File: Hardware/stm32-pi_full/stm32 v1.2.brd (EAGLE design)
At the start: 131.4 x 105.8 mm, 287 parts, among them J1 JUMPER-SMT_2_NC_TRACE_NO-SILK, Q1 PNP, Q2 NPN, Q3 NPN, U1 ESP32-WROOM-32D

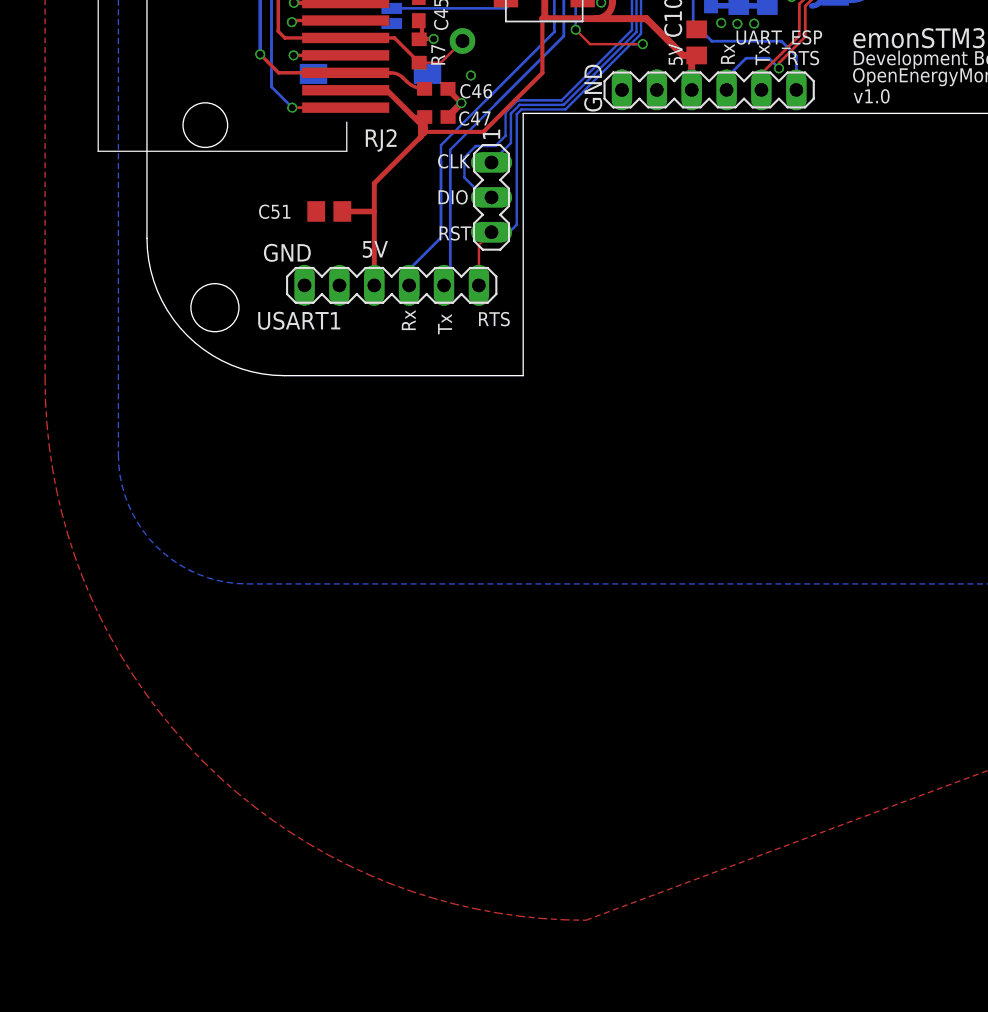
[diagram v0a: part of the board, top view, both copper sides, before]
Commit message: pulse detect fix. separated readings timer and posting timer implemented.
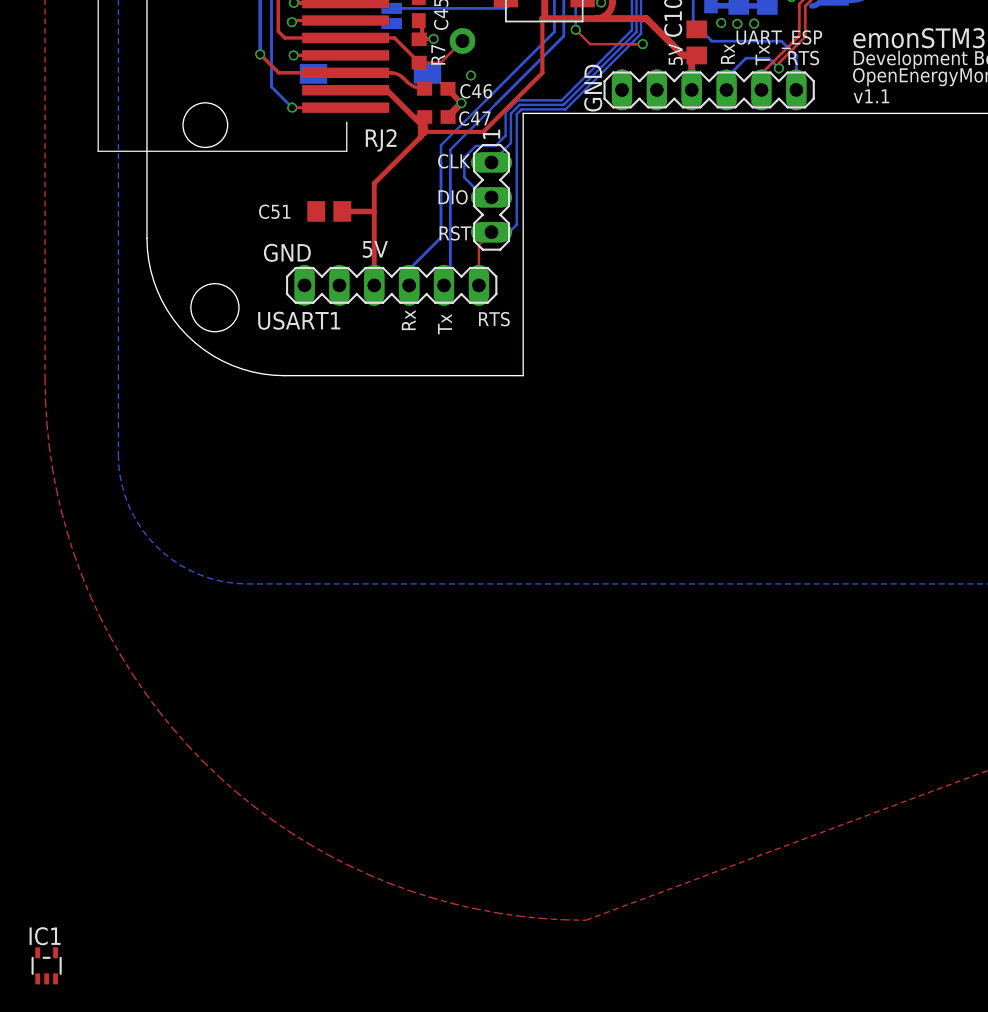
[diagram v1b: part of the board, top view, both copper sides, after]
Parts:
- added IC1: (no value), analog-devices:SC70-5
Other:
- board text added: "v1.1"
- board text removed: "v1.0"
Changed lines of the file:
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@@
 <text x="114.963" y="30.3" size="1.016" layer="26" font="vector" ratio="20" rot="MR0">Development Board</text>
 <text x="114.963" y="31.55" size="1.4224" layer="26" font="vector" ratio="20" rot="MR0">emonSTM32</text>
-<text x="114.881" y="27.409603125" size="1.016" layer="26" font="vector" ratio="20" rot="MR0">v1.0</text>
+<text x="114.881" y="27.409603125" size="1.016" layer="26" font="vector" ratio="20" rot="MR0">v1.1</text>
 <text x="97.91875" y="78.90644375" size="1.016" layer="21" font="vector" ratio="15" rot="SR0" align="bottom-center">Designed in </text>
 <text x="98.0209125" y="73.66226875" size="1.016" layer="21" font="vector" ratio="15" rot="SR0" align="bottom-center">North Wales </text>
@@
 <text x="51.35315" y="22.618528125" size="1.016" layer="25" font="vector" ratio="20">Development Board</text>
 <text x="51.35315" y="23.868528125" size="1.4224" layer="25" font="vector" ratio="20">emonSTM32</text>
-<text x="51.43515" y="19.837603125" size="1.016" layer="25" font="vector" ratio="20">v1.0</text>
+<text x="51.43515" y="19.837603125" size="1.016" layer="25" font="vector" ratio="20">v1.1</text>
 <hole x="14.3" y="79.2" drill="3.18"/>
 <circle x="14.3" y="79.2" radius="3.5" width="0.1" layer="21"/>
@@
 </element>
 <element name="TP12" library="SparkFun-Connectors" package="PAD.03X.03" value="TEST-POINT3" x="80.217515625" y="39.5264625" smashed="yes"/>
+<element name="IC1" library="analog-devices" library_urn="urn:adsk.eagle:library:102" package="SC70-5" package3d_urn="urn:adsk.eagle:package:3966/1" value="" x="-7.30681875" y="-42.983403125" smashed="yes">
+<attribute name="MF" value="" x="-7.30681875" y="-42.983403125" size="1.778" layer="27" display="off"/>
+<attribute name="MPN" value="" x="-7.30681875" y="-42.983403125" size="1.778" layer="27" display="off"/>
+<attribute name="NAME" x="-8.70381875" y="-41.459403125" size="1.27" layer="25"/>
+<attribute name="OC_FARNELL" value="unknown" x="-7.30681875" y="-42.983403125" size="1.778" layer="27" display="off"/>
+<attribute name="OC_NEWARK" value="unknown" x="-7.30681875" y="-42.983403125" size="1.778" layer="27" display="off"/>
+<attribute name="POPULARITY" value="0" x="-7.30681875" y="-42.983403125" size="1.778" layer="27" display="off"/>
+<attribute name="VALUE" x="-8.95781875" y="-45.777403125" size="1.27" layer="27"/>
+</element>
 </elements>
 <signals>

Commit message: modified:   Hardware/stm32-pi_full/stm32 v1.2.brd 	modified:   Hardware/stm32-pi_full/stm32 v1.2.sch 	modified:   Software/Sombrero_VE_Working6/build/Sombrero_VE_Working6.bin
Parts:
- removed C20: 2.2nF, rcl:C0603
- removed C35, C36: (no value), rcl:C0603
- removed C50: 1uF, rcl:C0603
- removed D10, D11, D12, D13, D15, D16, D19, D20, D24, D25, D27, D28, D29, D5, D6, D7, D8, D9: ESD5Z3.3T1G, microbuilder:SOD-523
- removed IC1, IC2: (no value), analog-devices:SC70-5
- removed JP11, JP13, JP15: JUMPER-SMT_2_NO_NO-SILK_ROUND, SparkFun-Jumpers:SMT-JUMPER_2_NO_NO-SILK_ROUND
- removed R23: 1k, resistor:R0603
- removed R38: 39k, resistor:R0603
- removed R46, R47, R48: 0R, rcl:R0603
- removed R54: 10k, resistor:R0603
- removed R6: 0R, resistor:R0603
- removed RB1B, RB2B, RB3B, RB4B, RB5B, RB6B, RB7B, RB8B, RB9B: (no value), rcl:R0805
- removed RB4A, RB5A, RB6A: 6R8, rcl:R0805
- removed TP3, TP5, TP6: TEST-POINTPOGO_PTH, SparkFun-Connectors:1X01_NO_SILK
- added LMV1, LMV2, LMV3: LMV824IDG4, LMV824IDG4:SOIC127P600X175-14N
- added RB11, RB12, RB13: 510R, rcl:R0805
- added RB4, RB5, RB6: 6R8, rcl:R0805
- added RB44, RB55, RB66: 680R, rcl:R0805
- added SJ1: JUMPER-SMT_2_NC_TRACE_NO-SILK, SparkFun-Jumpers:SMT-JUMPER_2_NC_TRACE_NO-SILK
- added U2: RFM69HCW/RFM95W, microbuilder:RFMHCW_SMT
- R55: value 91k -> 10k
- moved D3 127.8 mm to (12.0, -50.0)
- moved D2 123.2 mm to (12.0, -43.2), turned to 0 degrees
- moved TP8 10.6 mm to (53.2, 64.4)
- moved TP2 8.19 mm to (57.4, 65.1)
- moved R55 6.84 mm to (53.3, 61.7), turned to 90 degrees
- moved TP18 3.84 mm to (88.8, 74.6)
- moved C53 3.33 mm to (50.0, 60.8)
- moved TP19 2.88 mm to (58.1, 76.5)
- moved RB4_ 2.57 mm to (78.4, 88.2)
- moved RB5_ 2.54 mm to (65.8, 88.2)
- moved RB6_ 2.49 mm to (53.1, 88.1)
- moved R56 1.88 mm to (52.4, 58.5), turned to 0 degrees
- moved RF2 1.45 mm to (80.8, 75.0), turned to 0 degrees
- moved RF5 1.43 mm to (65.9, 75.0), turned to 0 degrees
- moved RF7 1.42 mm to (56.0, 75.0), turned to 0 degrees
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- renumbered RB1A to RB1, RB2A to RB2, RB3A to RB3, RB7A to RB7, RB8A to RB8, RB9A to RB9
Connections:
- net CT4 renamed CT4_ADC
- net CT5 renamed CT5_ADC
- net CT6 renamed CT6_ADC
- removed net N$25: R46.2, RB6A.2, RB6B.2, RB6_.2
- new net BIAS1: D2.2, D3.1
- new net BIAS456: LMV2.10, LMV2.13, LMV2.14, LMV2.3, LMV2.5, RB44.2, RB55.2, RB66.2
- new net CT4_OUT: LMV2.1, RB11.1, RF4.1
- new net CT5_OUT: LMV2.7, RB12.1, RF5.1
- new net CT6_OUT: LMV2.8, RB13.2, RF6.1
- new net N$12: CT5.P$3
- new net N$38: CT4.P$3
- new net N$40: CT6.P$1, RB6.2, RB66.1, RB6_.2
- net +3V3ANA: now also LMV1.4, LMV2.4, LMV3.4; no longer D15.K, D16.K, D19.K, D20.K, D24.K, D25.K, D27.K, D28.K, D29.K, IC2.5
- net AGND: now also LMV1.11, LMV2.11, LMV3.11; no longer C35.2, C36.2, C50.2, D10.A, D11.A, D12.A, D13.A, D5.A, D6.A, D7.A, D8.A, D9.A, IC2.2, R54.2
- net BIAS: now also LMV2.12; no longer C35.1, C36.1, CT4.P$1, CT5.P$1, CT6.P$1, D2.2, D3.1, JP11.1, JP13.1, JP15.1, R23.2, R38.1, R46.1, R47.1, R48.1, R6.2, TP3.1
- net CT_IN1: no longer D13.K, D29.A, RB1B.1
- net CT_IN2: no longer D12.K, D28.A, RB2B.1
- net CT_IN3: no longer D11.K, D27.A, RB3B.1
- net CT_IN4: now also LMV2.2, RB11.2, RB4.1; no longer D10.K, D25.A, RB4A.1, RB4B.1, RF4.1
- net CT_IN5: now also LMV2.6, RB12.2, RB5.1; no longer D20.A, D9.K, RB5A.1, RB5B.1, RF5.1
- net CT_IN6: now also LMV2.9, RB13.1, RB6.1; no longer D24.A, D8.K, RB6A.1, RB6B.1, RF6.1
- net CT_IN7: no longer D19.A, D7.K, RB7B.1
- net CT_IN8: no longer D16.A, D6.K, RB8B.1
- net CT_IN9: no longer D15.A, D5.K, RB9B.1
- net DGND: now also U2.16P, U2.2P, U2.9P
- net N$10: no longer JP13.2
- net N$2: no longer JP11.2
- net N$20: no longer JP15.2
- net N$24: now also CT6.P$3; no longer R47.2, RB5A.2, RB5B.2, RB5_.2
- net N$26: no longer RB1B.2
- net N$27: no longer RB2B.2
- net N$29: no longer RB8B.2
- net N$34: no longer RB9B.2
- net N$35: now also CT4.P$1, RB4.2, RB44.1; no longer R48.2, RB4A.2, RB4B.2
- net N$36: no longer RB7B.2
- net N$37: no longer RB3B.2
- net N$7: now also CT5.P$1, RB5.2, RB55.1, RB5_.2; no longer C50.1, R23.1
- net OPAMP_INVERT-: now also SJ1.1; no longer C20.1, IC2.4, R38.2, R54.1, TP6.1
- net OPAMP_NON-INVERT+: no longer IC2.3, TP2.1
- net OPAMP_OUT: now also SJ1.2, TP2.1; no longer C20.2, IC2.1, R6.1, TP5.1
- net VDD: now also U2.5P
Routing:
- net BIAS: track 525.0 -> 26.7 mm, vias 4 -> 0
- net BIAS456: track 0.00 -> 67.5 mm, vias 0 -> 3
- net +3V3ANA: track 73.2 -> 35.3 mm, vias 23 -> 13
- net CT_IN3: track 37.3 -> 0.00 mm
- net N$40: track 0.00 -> 26.0 mm
- net N$7: track 2.18 -> 25.9 mm
- net CT5_OUT: track 0.00 -> 15.7 mm
- net CT4_OUT: track 0.00 -> 13.9 mm
- net N$35: track 11.1 -> 23.9 mm
- net OPAMP_OUT: track 17.4 -> 5.57 mm
- net VREF+: track 53.1 -> 41.5 mm
- net CT_IN5: track 29.6 -> 18.3 mm, vias 0 -> 2
- net N$25: track 11.2 -> 0.00 mm
- net OPAMP_NON-INVERT+: track 18.4 -> 7.42 mm, vias 1 -> 0
- net N$24: track 10.9 -> 0.00 mm
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
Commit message: update
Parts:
- RB1, RB2, RB3, RB4, RB5, RB6, RB7, RB8, RB9: value 6R8 -> 6R81
- RB11, RB12, RB13: value 510R -> 510R 0.1%
- RB44, RB55, RB66: value 680R -> 680R | 681R 0.1%

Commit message: brd changes
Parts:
- removed JP10, JP12, JP14, JP16, JP17, JP18: JUMPER-SMT_2_NO_NO-SILK_ROUND, SparkFun-Jumpers:SMT-JUMPER_2_NO_NO-SILK_ROUND
- removed R42, R44, R45, R49, R50, R51: 0R, rcl:R0603
- added RB10, RB14, RB15, RB16, RB17, RB18: 510R 0.1%, rcl:R0805
- added RB19, RB20, RB21, RB22, RB23, RB24: 680R | 681R 0.1%, rcl:R0805
- moved LMV1 168.7 mm to (93.9, 81.6), turned to 270 degrees
- moved LMV3 148.0 mm to (37.3, 81.5), turned to 270 degrees
- moved D2 68.5 mm to (52.4, 12.1)
- moved D3 68.5 mm to (52.4, 5.32)
- moved RB1 3.89 mm to (116.6, 88.2)
- moved RB2 3.89 mm to (103.8, 88.2)
- moved RB3 3.89 mm to (91.3, 88.2)
- moved RB8 3.85 mm to (27.5, 88.1)
- moved RB9 3.81 mm to (14.8, 88.1)
- moved RB7 3.81 mm to (40.1, 88.1)
- moved RB1_ 2.54 mm to (116.6, 88.2)
- moved RB2_ 2.54 mm to (103.8, 88.2)
- moved RB3_ 2.54 mm to (91.3, 88.2)
- moved RB8_ 2.45 mm to (27.5, 88.1)
- moved RB9_ 2.45 mm to (14.8, 88.1)
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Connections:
- net CT1 renamed CT1_ADC
- net CT2 renamed CT2_ADC
- net CT3 renamed CT3_ADC
- removed net N$29: R50.2, RB8.2, RB8_.2
- removed net N$34: R51.2, RB9.2, RB9_.2
- removed net N$37: R45.2, RB3.2, RB3_.2
- new net BIAS123: LMV1.10, LMV1.13, LMV1.14, LMV1.3, LMV1.5, RB19.2, RB20.2, RB21.2
- new net BIAS789: LMV3.10, LMV3.13, LMV3.14, LMV3.3, LMV3.5, RB22.2, RB23.2, RB24.2
- new net CT1_OUT: LMV1.1, RB10.1, RF1.1
- new net CT2_OUT: LMV1.7, RB14.1, RF2.1
- new net CT3_OUT: LMV1.8, RB15.2, RF3.1
- new net CT7_OUT: LMV3.1, RB16.1, RF7.1
- new net CT8_OUT: LMV3.7, RB17.1, RF8.1
- new net CT9_OUT: LMV3.8, RB18.2, RF9.1
- new net N$43: CT9.P$1, RB24.1, RB9.2, RB9_.2
- new net N$45: CT8.P$1, RB23.1, RB8.2, RB8_.2
- new net N$46: CT7.P$1, RB22.1, RB7.2, RB7_.2
- net BIAS: now also LMV1.12, LMV3.12; no longer CT1.P$1, CT2.P$1, CT3.P$1, CT7.P$1, CT8.P$1, CT9.P$1, JP10.1, JP12.1, JP14.1, JP16.1, JP17.1, JP18.1, R42.1, R44.1, R45.1, R49.1, R50.1, R51.1
- net CT_IN1: now also LMV1.2, RB10.2; no longer RF1.1
- net CT_IN2: now also LMV1.6, RB14.2; no longer RF2.1
- net CT_IN3: now also LMV1.9, RB15.1; no longer RF3.1
- net CT_IN7: now also LMV3.2, RB16.2; no longer RF7.1
- net CT_IN8: now also LMV3.6, RB17.2; no longer RF8.1
- net CT_IN9: now also LMV3.9, RB18.1; no longer RF9.1
- net N$1: no longer JP10.2
- net N$13: no longer JP14.2
- net N$21: no longer JP16.2
- net N$22: no longer JP17.2
- net N$23: no longer JP18.2
- net N$26: now also CT1.P$1, RB19.1; no longer R42.2
- net N$27: now also CT2.P$1, RB20.1; no longer R44.2
- net N$36: now also CT3.P$1, RB21.1, RB3.2, RB3_.2; no longer R49.2, RB7.2, RB7_.2
- net N$8: no longer JP12.2
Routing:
- net BIAS123: track 0.00 -> 72.0 mm, vias 0 -> 2
- net BIAS789: track 0.00 -> 61.6 mm, vias 0 -> 3
- net CT_IN3: track 0.00 -> 28.2 mm, vias 0 -> 1
- net CT_IN8: track 49.7 -> 22.5 mm
- net CT8_OUT: track 0.00 -> 26.2 mm
- net N$45: track 0.00 -> 25.2 mm
- net N$43: track 0.00 -> 25.0 mm
- net N$46: track 0.00 -> 24.9 mm
- net CT1_OUT: track 0.00 -> 22.5 mm, vias 0 -> 2
- net CT3_OUT: track 0.00 -> 18.2 mm
- net CT7_OUT: track 0.00 -> 17.6 mm
- net CT_IN2: track 44.3 -> 26.6 mm, vias 0 -> 1
- net CT_IN7: track 44.0 -> 26.6 mm
- net CT9_OUT: track 0.00 -> 16.7 mm
- net N$36: track 9.77 -> 25.4 mm
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
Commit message: update
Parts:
- removed C53: 22uF, rcl:C0805
- added C20, C35: 22uF, rcl:C0805
- added FB10, FB11, FB6: (no value), microbuilder:_0603
- added IC1: TS461CLT, TS461CLT:SOT95P280X145-5N
- added JP3, JP5: JUMPER-SMT_3_1-NC_TRACE_NO-SILK, SparkFun-Jumpers:SMT-JUMPER_3_1-NC_TRACE_NO-SILK
- added JP6: JUMPER-SMT_2_NC_PASTE_SILK, SparkFun-Jumpers:SMT-JUMPER_2_NC_PASTE_SILK
- added R6: 20R, rcl:R0603
- added TP3, TP5, TP6: TEST-POINTPOGO_PTH, SparkFun-Connectors:1X01_NO_SILK
- C11, C23: value 1uF -> 22uf
- FB1: value (none) -> 1600R
- FB2: value (none) -> 0R
- moved D3 73.4 mm to (50.7, 78.7)
- moved D2 69.6 mm to (50.5, 81.6), turned to 180 degrees
- moved R56 2.91 mm to (50.3, 60.5), turned to 90 degrees
- moved C33 1.77 mm to (107.7, 34.6)
- moved TP2 1.67 mm to (56.4, 66.5)
- moved R55 0.50 mm to (52.9, 62.1), turned to 0 degrees
- moved TP8 0.45 mm to (53.7, 64.5)
- moved C11 0.35 mm to (93.7, 67.4)
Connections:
- removed net BIAS1: D2.2, D3.1
- removed net OPAMP_NON-INVERT+: C53.1, R55.1, R56.2, STM32F303VE.58
- new net ANT_LORA: JP6.1, U2.1P
- new net BIAS_SOT23: IC1.1, IC1.4, JP5.2
- new net DIO1_RFM: STM32F303VE.3, U2.7P
- new net N$25: FB10.1, MCP1825.3
- new net N$29: C11.1, C37.1, FB6.1, REF19X.2, REF19X.3, TP11.1
- new net N$34: FB11.1, MCP1825(ANALOG).3
- new net N$37: JP3.2, R55.1, R56.2
- new net N$39: C20.1, IC1.3, JP3.3, TP6.1
- new net N$42: JP5.3, R6.1, TP3.1
- new net STM32_OPAMP_NON-INVERT+: C35.1, JP3.1, STM32F303VE.58
- new net STM32_OPAMP_OUT: JP5.1, STM32F303VE.51, TP2.1
- net +3V3: now also FB10.2; no longer MCP1825.3
- net +3V3ANA: now also FB11.2, FB6.2, IC1.2; no longer C11.1, C37.1, MCP1825(ANALOG).3, REF19X.2, REF19X.3, TP11.1
- net AGND: now also C20.2, C35.2, IC1.5; no longer C53.2
- net ANT: now also JP6.2
- net BIAS: now also D2.2, D3.1, R6.2, TP5.1
- net DGND: no longer U2.16P, U2.2P
- net DIO0_RFM: now also U2.6P
- net OPAMP_OUT: no longer STM32F303VE.51, TP2.1
- net RGND: now also U2.16P, U2.2P
- net RST_RFM: now also U2.14P
- net SPI4_CLK_MASTER: now also U2.12P
- net SPI4_CS_RFM69_MASTER: now also U2.13P
- net SPI4_MISO_MASTER: now also U2.10P
- net SPI4_MOSI_MASTER: now also U2.11P
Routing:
- net BIAS: track 18.3 -> 159.3 mm, vias 0 -> 8
- net DIO1_RFM: track 0.00 -> 39.9 mm, vias 0 -> 3
- net VDD: track 11.5 -> 30.7 mm, vias 0 -> 3
- net RST_RFM: track 51.2 -> 68.7 mm, vias 2 -> 4
- net STM32_OPAMP_OUT: track 0.00 -> 16.2 mm, vias 0 -> 1
- net ANT_LORA: track 0.00 -> 15.5 mm, vias 0 -> 2
- net SPI4_MISO_MASTER: track 42.8 -> 58.2 mm, vias 2 -> 3
- net SPI4_CS_RFM69_MASTER: track 50.8 -> 64.1 mm, vias 2 -> 5
- net STM32_OPAMP_NON-INVERT+: track 0.00 -> 11.1 mm
- net N$29: track 0.00 -> 9.79 mm
- net OPAMP_NON-INVERT+: track 9.73 -> 0.00 mm
- net RGND: track 34.0 -> 43.0 mm, vias 22 -> 25
- net BIAS_SOT23: track 0.00 -> 6.73 mm
- net SPI4_CLK_MASTER: track 51.2 -> 57.6 mm, vias 2 -> 3
- net N$39: track 0.00 -> 5.98 mm
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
